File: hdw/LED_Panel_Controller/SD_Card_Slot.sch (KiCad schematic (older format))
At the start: 17 parts

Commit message: lots of schematic progress
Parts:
- J?: footprint (none) -> Connectors_Card:Hirose_DM3AT-SF-PEJM5; Digi-Key PN (none) -> HR1964CT-ND
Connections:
- net SD_SPI_SDI renamed SD_SPI_MISO
- net SD_SPI_SDO renamed SD_SPI_MOSI
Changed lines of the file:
@@
 encoding utf-8
 Sheet 16 34
-Title ""
-Date "2020-09-08"
-Rev ""
-Comp ""
+Title "LED Panel Controller"
+Date "2020-12-23"
+Rev "A"
+Comp "Drew Maatman, Logan Wedel"
 Comment1 ""
 Comment2 ""
@@
 F 0 "J?" H 7790 4750 50  0000 C CNN
 F 1 "Micro_SD_Card_Det_Hirose_DM3AT" H 7790 4650 50  0000 C CNN
-F 2 "" H 9890 4620 50  0001 C CNN
+F 2 "Connectors_Card:Hirose_DM3AT-SF-PEJM5" H 9890 4620 50  0001 C CNN
 F 3 "https://www.hirose.com/product/en/download_file/key_name/DM3/category/Catalog/doc_file_id/49662/?file_category_id=4&item_id=195&is_series=1" H 7840 4020 50  0001 C CNN
+F 4 "HR1964CT-ND" H 7840 3920 50  0001 C CNN "Digi-Key PN"
 	1    7840 3920
 	1    0    0    -1
@@
 L Custom_Library:R_Custom R?
 U 1 1 5F6EBBB2
-P 4300 2950
+P 4300 2960
 AR Path="/5D6B2673/5F6EBBB2" Ref="R?"  Part="1"
 AR Path="/5D6C0D23/5F6EBBB2" Ref="R?"  Part="1"
@@
 AR Path="/5F581B41/5F6EBBB2" Ref="R?"  Part="1"
 AR Path="/5F582E11/5F6EBBB2" Ref="R?"  Part="1"
-F 0 "R?" H 4210 2950 50  0000 R CNN
-F 1 "10k" V 4300 2880 50  0000 L CNN
-F 2 "Resistors_SMD:R_0402" H 4300 2950 50  0001 C CNN
-F 3 "" H 4300 2950 50  0001 C CNN
-F 4 "0402" H 4400 3020 50  0000 L CNN "display_footprint"
-F 5 "1%" H 4400 2920 50  0000 L CNN "Tolerance"
-F 6 "1/16W" H 4400 2820 50  0000 L CNN "Wattage"
-F 7 "" H 4600 3350 60  0001 C CNN "Digi-Key PN"
-	1    4300 2950
+F 0 "R?" H 4210 2960 50  0000 R CNN
+F 1 "10k" V 4300 2890 50  0000 L CNN
+F 2 "Resistors_SMD:R_0402" H 4300 2960 50  0001 C CNN
+F 3 "" H 4300 2960 50  0001 C CNN
+F 4 "0402" H 4400 3030 50  0000 L CNN "display_footprint"
+F 5 "1%" H 4400 2930 50  0000 L CNN "Tolerance"
+F 6 "1/16W" H 4400 2830 50  0000 L CNN "Wattage"
+F 7 "" H 4600 3360 60  0001 C CNN "Digi-Key PN"
+	1    4300 2960
 	-1   0    0    -1
 $EndComp
@@
 	-1   0    0    -1
 $EndComp
-Text GLabel 3050 3620 0    50   Input ~ 0
+Text GLabel 3010 3620 0    50   Input ~ 0
 SD_SPI_CS
-Text GLabel 3050 3720 0    50   Input ~ 0
-SD_SPI_SDO
-Text GLabel 3050 3920 0    50   Input ~ 0
+Text GLabel 3010 3720 0    50   Input ~ 0
+SD_SPI_MOSI
+Text GLabel 3010 3920 0    50   Input ~ 0
 SD_SPI_SCK
 Text GLabel 3010 4120 0    50   Output ~ 0
-SD_SPI_SDI
-Text GLabel 3050 4320 0    50   Input ~ 0
+SD_SPI_MISO
+Text GLabel 3010 4320 0    50   Output ~ 0
 SD_CARD_DET
 Wire Wire Line
-	3770 2810 4300 2810
-Wire Wire Line
-	4300 2810 4300 2800
-Wire Wire Line
-	4300 2810 4560 2810
-Connection ~ 4300 2810
-Wire Wire Line
-	4560 2560 4560 2810
-Connection ~ 4560 2810
-Wire Wire Line
-	4560 2810 4850 2810
-Wire Wire Line
 	3770 3110 3770 3620
 Wire Wire Line
 	3770 3620 4480 3620
 Wire Wire Line
-	4300 3100 4300 3720
-Wire Wire Line
-	3050 3620 3770 3620
+	4300 3110 4300 3720
+Wire Wire Line
+	3010 3620 3770 3620
 Connection ~ 3770 3620
 Wire Wire Line
-	3050 3720 4300 3720
+	3010 3720 4300 3720
 $Comp
 L Custom_Library:R_Custom R?
@@
 $EndComp
 Wire Wire Line
-	3050 3920 3230 3920
+	3010 3920 3230 3920
 $Comp
 L Custom_Library:R_Custom R?
@@
 	4980 3920 4850 3920
 Wire Wire Line
-	3050 4320 5940 4320
+	3010 4320 5940 4320
 Wire Wire Line
 	3010 4120 5400 4120
@@
 $EndComp
 Wire Wire Line
-	5940 2810 5400 2810
-Wire Wire Line
-	5400 2810 4850 2810
-Connection ~ 5400 2810
-Connection ~ 4850 2810
-Wire Wire Line
 	5480 5440 5480 4120
 Connection ~ 5480 4120
@@
 L power:+3.3V #PWR?
 U 1 1 5F70F685
-P 4560 2560
+P 3770 2810
 AR Path="/5CB7718D/5F70F685" Ref="#PWR?"  Part="1"
 AR Path="/5E0DC082/5F70F685" Ref="#PWR?"  Part="1"
@@
 AR Path="/5F581B64/5F70F685" Ref="#PWR?"  Part="1"
 AR Path="/5F582E11/5F70F685" Ref="#PWR?"  Part="1"
-F 0 "#PWR?" H 4560 2410 50  0001 C CNN
-F 1 "+3.3V" H 4560 2700 50  0000 C CNN
-F 2 "" H 4560 2560 50  0001 C CNN
-F 3 "" H 4560 2560 50  0001 C CNN
-	1    4560 2560
+F 0 "#PWR?" H 3770 2660 50  0001 C CNN
+F 1 "+3.3V" H 3770 2950 50  0000 C CNN
+F 2 "" H 3770 2810 50  0001 C CNN
+F 3 "" H 3770 2810 50  0001 C CNN
+	1    3770 2810
 	1    0    0    -1
 $EndComp
@@
 Wire Wire Line
 	8760 4420 8640 4420
+$Comp
+L power:+3.3V #PWR?
+U 1 1 5FE67F76
+P 4300 2810
+AR Path="/5CB7718D/5FE67F76" Ref="#PWR?"  Part="1"
+AR Path="/5E0DC082/5FE67F76" Ref="#PWR?"  Part="1"
+AR Path="/5E0F263A/5FE67F76" Ref="#PWR?"  Part="1"
+AR Path="/5EAE2D8A/5FE67F76" Ref="#PWR?"  Part="1"
+AR Path="/5F581B64/5FE67F76" Ref="#PWR?"  Part="1"
+AR Path="/5F582E11/5FE67F76" Ref="#PWR?"  Part="1"
+F 0 "#PWR?" H 4300 2660 50  0001 C CNN
+F 1 "+3.3V" H 4300 2950 50  0000 C CNN
+F 2 "" H 4300 2810 50  0001 C CNN
+F 3 "" H 4300 2810 50  0001 C CNN
+	1    4300 2810
+	1    0    0    -1
+$EndComp
+$Comp
+L power:+3.3V #PWR?
+U 1 1 5FE6815E
+P 4850 2810
+AR Path="/5CB7718D/5FE6815E" Ref="#PWR?"  Part="1"
+AR Path="/5E0DC082/5FE6815E" Ref="#PWR?"  Part="1"
+AR Path="/5E0F263A/5FE6815E" Ref="#PWR?"  Part="1"
+AR Path="/5EAE2D8A/5FE6815E" Ref="#PWR?"  Part="1"
+AR Path="/5F581B64/5FE6815E" Ref="#PWR?"  Part="1"
+AR Path="/5F582E11/5FE6815E" Ref="#PWR?"  Part="1"
+F 0 "#PWR?" H 4850 2660 50  0001 C CNN
+F 1 "+3.3V" H 4850 2950 50  0000 C CNN
+F 2 "" H 4850 2810 50  0001 C CNN
+F 3 "" H 4850 2810 50  0001 C CNN
+	1    4850 2810
+	1    0    0    -1
+$EndComp
+$Comp
+L power:+3.3V #PWR?
+U 1 1 5FE6833E
+P 5400 2810
+AR Path="/5CB7718D/5FE6833E" Ref="#PWR?"  Part="1"
+AR Path="/5E0DC082/5FE6833E" Ref="#PWR?"  Part="1"
+AR Path="/5E0F263A/5FE6833E" Ref="#PWR?"  Part="1"
+AR Path="/5EAE2D8A/5FE6833E" Ref="#PWR?"  Part="1"
+AR Path="/5F581B64/5FE6833E" Ref="#PWR?"  Part="1"
+AR Path="/5F582E11/5FE6833E" Ref="#PWR?"  Part="1"
+F 0 "#PWR?" H 5400 2660 50  0001 C CNN
+F 1 "+3.3V" H 5400 2950 50  0000 C CNN
+F 2 "" H 5400 2810 50  0001 C CNN
+F 3 "" H 5400 2810 50  0001 C CNN
+	1    5400 2810
+	1    0    0    -1
+$EndComp
+$Comp
+L power:+3.3V #PWR?
+U 1 1 5FE684D9
+P 5940 2810
+AR Path="/5CB7718D/5FE684D9" Ref="#PWR?"  Part="1"
+AR Path="/5E0DC082/5FE684D9" Ref="#PWR?"  Part="1"
+AR Path="/5E0F263A/5FE684D9" Ref="#PWR?"  Part="1"
+AR Path="/5EAE2D8A/5FE684D9" Ref="#PWR?"  Part="1"
+AR Path="/5F581B64/5FE684D9" Ref="#PWR?"  Part="1"
+AR Path="/5F582E11/5FE684D9" Ref="#PWR?"  Part="1"
+F 0 "#PWR?" H 5940 2660 50  0001 C CNN
+F 1 "+3.3V" H 5940 2950 50  0000 C CNN
+F 2 "" H 5940 2810 50  0001 C CNN
+F 3 "" H 5940 2810 50  0001 C CNN
+	1    5940 2810
+	1    0    0    -1
+$EndComp
 $EndSCHEMATC

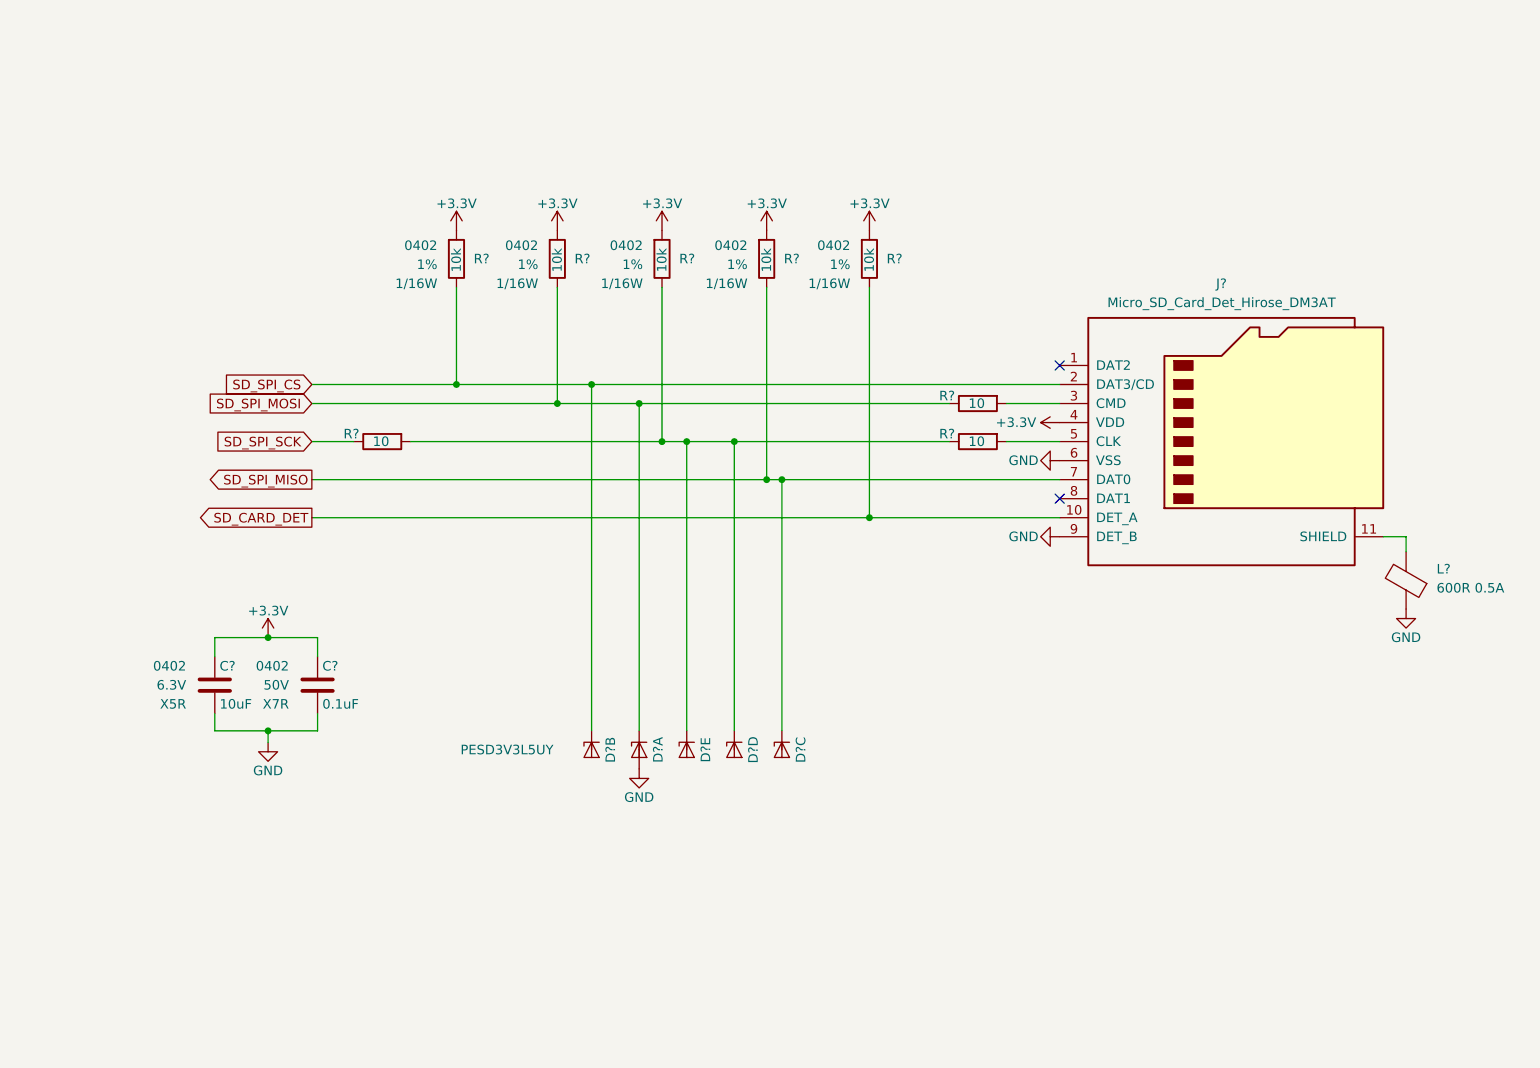
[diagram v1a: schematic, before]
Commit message: assigned a lot of nets to MCU pins
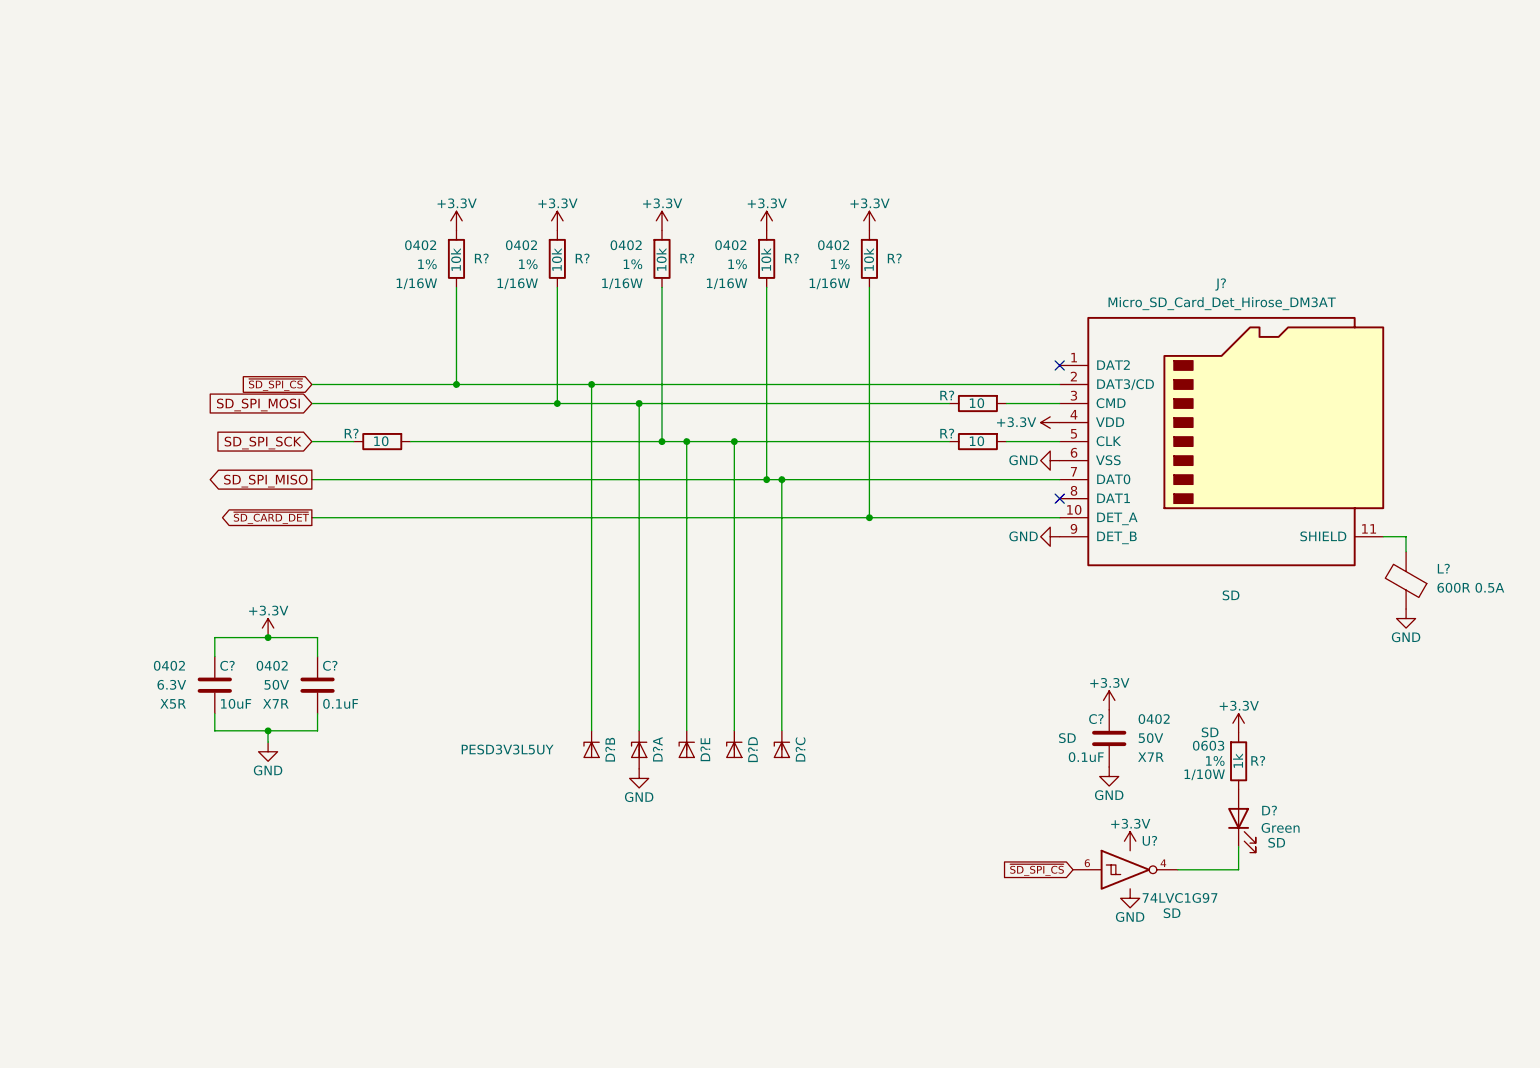
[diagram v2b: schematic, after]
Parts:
- added C?: 0.1uF, Capacitors_SMD:C_0402, symbol Custom_Library:C_Custom
- added D?: Green, LEDs:LED_0603, symbol Device:LED
- added R?: 1k, Resistors_SMD:R_0603, symbol Custom_Library:R_Custom
- added U?: 74LVC1G97, Package_TO_SOT_SMD:SOT-363_SC-70-6, symbol Custom_Library:74LVC1G97_Power_NOT
- J?: Configuration (none) -> SD
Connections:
- net +3V3: now also C?.1, R?.1, U?.1 (VCC), U?.5 (VCC)
- net GND: now also C?.2, U?.2 (GND), U?.3 (GND)
- net SD_CARD_DET renamed ~SD_CARD_DET
- net SD_SPI_CS renamed ~SD_SPI_CS
- net ~SD_SPI_CS: now also U?.6
- new net: D?.1 (K), U?.4
- new net: D?.2 (A), R?.2
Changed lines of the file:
@@
 F 3 "https://www.hirose.com/product/en/download_file/key_name/DM3/category/Catalog/doc_file_id/49662/?file_category_id=4&item_id=195&is_series=1" H 7840 4020 50  0001 C CNN
 F 4 "HR1964CT-ND" H 7840 3920 50  0001 C CNN "Digi-Key PN"
+F 5 "SD" H 7840 3110 50  0000 C CNN "Configuration"
 	1    7840 3920
 	1    0    0    -1
@@
 	-1   0    0    -1
 $EndComp
-Text GLabel 3010 3620 0    50   Input ~ 0
-SD_SPI_CS
+Text GLabel 3010 3620 0    40   Input ~ 0
+~SD_SPI_CS
 Text GLabel 3010 3720 0    50   Input ~ 0
 SD_SPI_MOSI
@@
 Text GLabel 3010 4120 0    50   Output ~ 0
 SD_SPI_MISO
-Text GLabel 3010 4320 0    50   Output ~ 0
-SD_CARD_DET
+Text GLabel 3010 4320 0    40   Output ~ 0
+~SD_CARD_DET
 Wire Wire Line
 	3770 3110 3770 3620
@@
 	1    0    0    -1
 $EndComp
+$Comp
+L power:+3.3V #PWR?
+U 1 1 601C2224
+P 7200 5330
+AR Path="/5F582E50/601C2224" Ref="#PWR?"  Part="1"
+AR Path="/5F5829C2/601C2224" Ref="#PWR?"  Part="1"
+AR Path="/5F582E44/601C2224" Ref="#PWR?"  Part="1"
+AR Path="/5F582E11/601C2224" Ref="#PWR?"  Part="1"
+F 0 "#PWR?" H 7200 5180 50  0001 C CNN
+F 1 "+3.3V" H 7200 5470 50  0000 C CNN
+F 2 "" H 7200 5330 50  0001 C CNN
+F 3 "" H 7200 5330 50  0001 C CNN
+	1    7200 5330
+	1    0    0    -1
+$EndComp
+$Comp
+L power:GND #PWR?
+U 1 1 601C222A
+P 7200 5630
+AR Path="/5F582E50/601C222A" Ref="#PWR?"  Part="1"
+AR Path="/5F5829C2/601C222A" Ref="#PWR?"  Part="1"
+AR Path="/5F582E44/601C222A" Ref="#PWR?"  Part="1"
+AR Path="/5F582E11/601C222A" Ref="#PWR?"  Part="1"
+F 0 "#PWR?" H 7200 5380 50  0001 C CNN
+F 1 "GND" H 7200 5480 50  0000 C CNN
+F 2 "" H 7200 5630 50  0001 C CNN
+F 3 "" H 7200 5630 50  0001 C CNN
+	1    7200 5630
+	1    0    0    -1
+$EndComp
+$Comp
+L power:+3.3V #PWR?
+U 1 1 601C2230
+P 7310 6070
+AR Path="/5F582E50/601C2230" Ref="#PWR?"  Part="1"
+AR Path="/5F5829C2/601C2230" Ref="#PWR?"  Part="1"
+AR Path="/5F582E44/601C2230" Ref="#PWR?"  Part="1"
+AR Path="/5F582E11/601C2230" Ref="#PWR?"  Part="1"
+F 0 "#PWR?" H 7310 5920 50  0001 C CNN
+F 1 "+3.3V" H 7310 6210 50  0000 C CNN
+F 2 "" H 7310 6070 50  0001 C CNN
+F 3 "" H 7310 6070 50  0001 C CNN
+	1    7310 6070
+	1    0    0    -1
+$EndComp
+$Comp
+L power:GND #PWR?
+U 1 1 601C2236
+P 7310 6270
+AR Path="/5F582E50/601C2236" Ref="#PWR?"  Part="1"
+AR Path="/5F5829C2/601C2236" Ref="#PWR?"  Part="1"
+AR Path="/5F582E44/601C2236" Ref="#PWR?"  Part="1"
+AR Path="/5F582E11/601C2236" Ref="#PWR?"  Part="1"
+F 0 "#PWR?" H 7310 6020 50  0001 C CNN
+F 1 "GND" H 7310 6120 50  0000 C CNN
+F 2 "" H 7310 6270 50  0001 C CNN
+F 3 "" H 7310 6270 50  0001 C CNN
+	1    7310 6270
+	1    0    0    -1
+$EndComp
+Wire Wire Line
+	7560 6170 7880 6170
+Wire Wire Line
+	7880 6170 7880 6050
+$Comp
+L power:+3.3V #PWR?
+U 1 1 601C223F
+P 7880 5450
+AR Path="/5CB7A8BC/601C223F" Ref="#PWR?"  Part="1"
+AR Path="/5CB7A8C3/601C223F" Ref="#PWR?"  Part="1"
+AR Path="/5E93CC4E/601C223F" Ref="#PWR?"  Part="1"
+AR Path="/5F582E4A/601C223F" Ref="#PWR?"  Part="1"
+AR Path="/5F582E44/601C223F" Ref="#PWR?"  Part="1"
+AR Path="/5F582E11/601C223F" Ref="#PWR?"  Part="1"
+F 0 "#PWR?" H 7880 5300 50  0001 C CNN
+F 1 "+3.3V" H 7880 5590 50  0000 C CNN
+F 2 "" H 7880 5450 50  0001 C CNN
+F 3 "" H 7880 5450 50  0001 C CNN
+	1    7880 5450
+	1    0    0    -1
+$EndComp
+$Comp
+L Custom_Library:74LVC1G97_Power_NOT U?
+U 1 1 601C2246
+P 7310 6170
+AR Path="/5F582E44/601C2246" Ref="U?"  Part="1"
+AR Path="/5F582E11/601C2246" Ref="U?"  Part="1"
+F 0 "U?" H 7370 6320 50  0000 L CNN
+F 1 "74LVC1G97" H 7370 6020 50  0000 L CNN
+F 2 "Package_TO_SOT_SMD:SOT-363_SC-70-6" H 7360 6170 50  0001 C CNN
+F 3 "http://www.ti.com/lit/ds/symlink/sn74lvc1g97.pdf" H 7360 6170 50  0001 C CNN
+F 4 "SD" H 7530 5940 50  0000 C CNN "Configuration"
+	1    7310 6170
+	1    0    0    -1
+$EndComp
+$Comp
+L Device:LED D?
+U 1 1 601C224E
+P 7880 5900
+AR Path="/5BB844FD/601C224E" Ref="D?"  Part="1"
+AR Path="/5BF346B3/601C224E" Ref="D?"  Part="1"
+AR Path="/5BAAE1F3/601C224E" Ref="D?"  Part="1"
+AR Path="/5CAD2D97/601C224E" Ref="D?"  Part="1"
+AR Path="/5CB7A8BC/601C224E" Ref="D?"  Part="1"
+AR Path="/5CB7A8C3/601C224E" Ref="D?"  Part="1"
+AR Path="/5E93CC4E/601C224E" Ref="D?"  Part="1"
+AR Path="/5F582E4A/601C224E" Ref="D?"  Part="1"
+AR Path="/5F582E44/601C224E" Ref="D?"  Part="1"
+AR Path="/5F582E11/601C224E" Ref="D?"  Part="1"
+F 0 "D?" V 7919 5783 50  0000 R CNN
+F 1 "Green" V 7828 5783 50  0000 R CNN
+F 2 "LEDs:LED_0603" H 7880 5900 50  0001 C CNN
+F 3 "~" H 7880 5900 50  0001 C CNN
+F 4 "754-1121-1-ND" H 2720 -420 50  0001 C CNN "Digi-Key PN"
+F 5 "SD" V 7750 5700 50  0000 C CNN "Configuration"
+	1    7880 5900
+	0    -1   -1   0
+$EndComp
+$Comp
+L Custom_Library:R_Custom R?
+U 1 1 601C2259
+P 7880 5600
+AR Path="/5BAAE1F3/601C2259" Ref="R?"  Part="1"
+AR Path="/5BAAE1DC/601C2259" Ref="R?"  Part="1"
+AR Path="/5BAAE16C/601C2259" Ref="R?"  Part="1"
+AR Path="/5BB844FD/601C2259" Ref="R?"  Part="1"
+AR Path="/5BF346B3/601C2259" Ref="R?"  Part="1"
+AR Path="/5CAD2D97/601C2259" Ref="R?"  Part="1"
+AR Path="/5CB7A8BC/601C2259" Ref="R?"  Part="1"
+AR Path="/5CB7A8C3/601C2259" Ref="R?"  Part="1"
+AR Path="/5E93CC4E/601C2259" Ref="R?"  Part="1"
+AR Path="/5F582E4A/601C2259" Ref="R?"  Part="1"
+AR Path="/5F582E44/601C2259" Ref="R?"  Part="1"
+AR Path="/5F582E11/601C2259" Ref="R?"  Part="1"
+F 0 "R?" H 7820 5600 50  0000 R CNN
+F 1 "1k" V 7880 5600 50  0000 C CNN
+F 2 "Resistors_SMD:R_0603" H 7880 5600 50  0001 C CNN
+F 3 "" H 7880 5600 50  0001 C CNN
+F 4 "0603" H 7950 5680 50  0000 L CNN "display_footprint"
+F 5 "1%" H 7950 5600 50  0000 L CNN "Tolerance"
+F 6 "1/10W" H 7950 5530 50  0000 L CNN "Wattage"
+F 7 "311-1.00KHRCT-ND" H 8180 6000 60  0001 C CNN "Digi-Key PN"
+F 8 "SD" H 8030 5750 50  0000 C CNN "Configuration"
+	1    7880 5600
+	-1   0    0    -1
+$EndComp
+$Comp
+L Custom_Library:C_Custom C?
+U 1 1 601C2264
+P 7200 5480
+AR Path="/5BAAE1F3/601C2264" Ref="C?"  Part="1"
+AR Path="/5BAAE1CB/601C2264" Ref="C?"  Part="1"
+AR Path="/5BE48F98/601C2264" Ref="C?"  Part="1"
+AR Path="/5CAD2D97/601C2264" Ref="C?"  Part="1"
+AR Path="/5CB7A8BC/601C2264" Ref="C?"  Part="1"
+AR Path="/5E6AF016/601C2264" Ref="C?"  Part="1"
+AR Path="/5EAE4AE4/601C2264" Ref="C?"  Part="1"
+AR Path="/5F582E50/601C2264" Ref="C?"  Part="1"
+AR Path="/5F5829C2/601C2264" Ref="C?"  Part="1"
+AR Path="/5F582E44/601C2264" Ref="C?"  Part="1"
+AR Path="/5F582E11/601C2264" Ref="C?"  Part="1"
+F 0 "C?" H 7225 5580 50  0000 L CNN
+F 1 "0.1uF" H 7225 5380 50  0000 L CNN
+F 2 "Capacitors_SMD:C_0402" H 7238 5330 50  0001 C CNN
+F 3 "" H 7225 5580 50  0001 C CNN
+F 4 "490-10701-1-ND" H 7625 5980 60  0001 C CNN "Digi-Key PN"
+F 5 "0402" H 7050 5580 50  0000 R CNN "display_footprint"
+F 6 "50V" H 7050 5480 50  0000 R CNN "Voltage"
+F 7 "X7R" H 7050 5380 50  0000 R CNN "Dielectric"
+F 8 "SD" H 7420 5480 50  0000 C CNN "Configuration"
+	1    7200 5480
+	-1   0    0    -1
+$EndComp
+Text GLabel 7010 6170 0    40   Input ~ 0
+~SD_SPI_CS
 $EndSCHEMATC

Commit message: more schematic development
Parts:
- removed R? (x5): 10k, Resistors_SMD:R_0402, symbol Custom_Library:R_Custom
- added R? (x5): 10k, Resistors_SMD:R_0402, symbol Custom_Library:R_Custom
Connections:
- net +3V3: now also R?.1, R?.1, R?.1, R?.1, R?.1
- net SD_SPI_MISO: now also D?.5 (K4), R?.2; no longer D?.4 (K3)
- net SD_SPI_MOSI: now also R?.2
- net ~SD_CARD_DET: now also D?.4 (K3), R?.2
- net ~SD_SPI_CS: now also R?.2
- net at D?.6 (K5), R?.1, R?.2: now also R?.2; no longer D?.5 (K4)
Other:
- moved on the sheet: C?, D?, D?A, D?B, D?C, D?D, D?E, J?, L?, R?, U?
